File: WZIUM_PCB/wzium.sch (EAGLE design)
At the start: 5 parts, among them J2 RASPBERRYPI-40-PIN-GPIO_PTH_M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

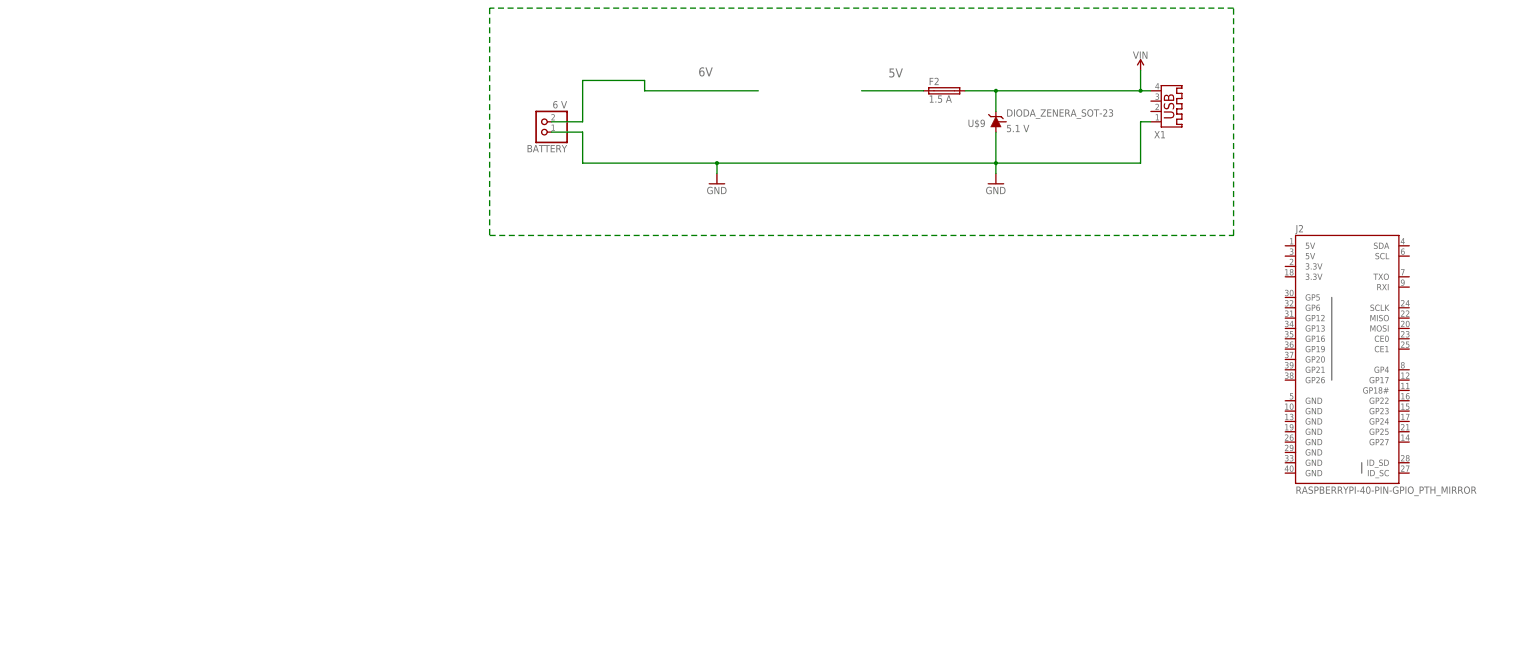
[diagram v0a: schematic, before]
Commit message: dodanie sekcji sterowania silnikiem i AVR, dodanie .gitignore
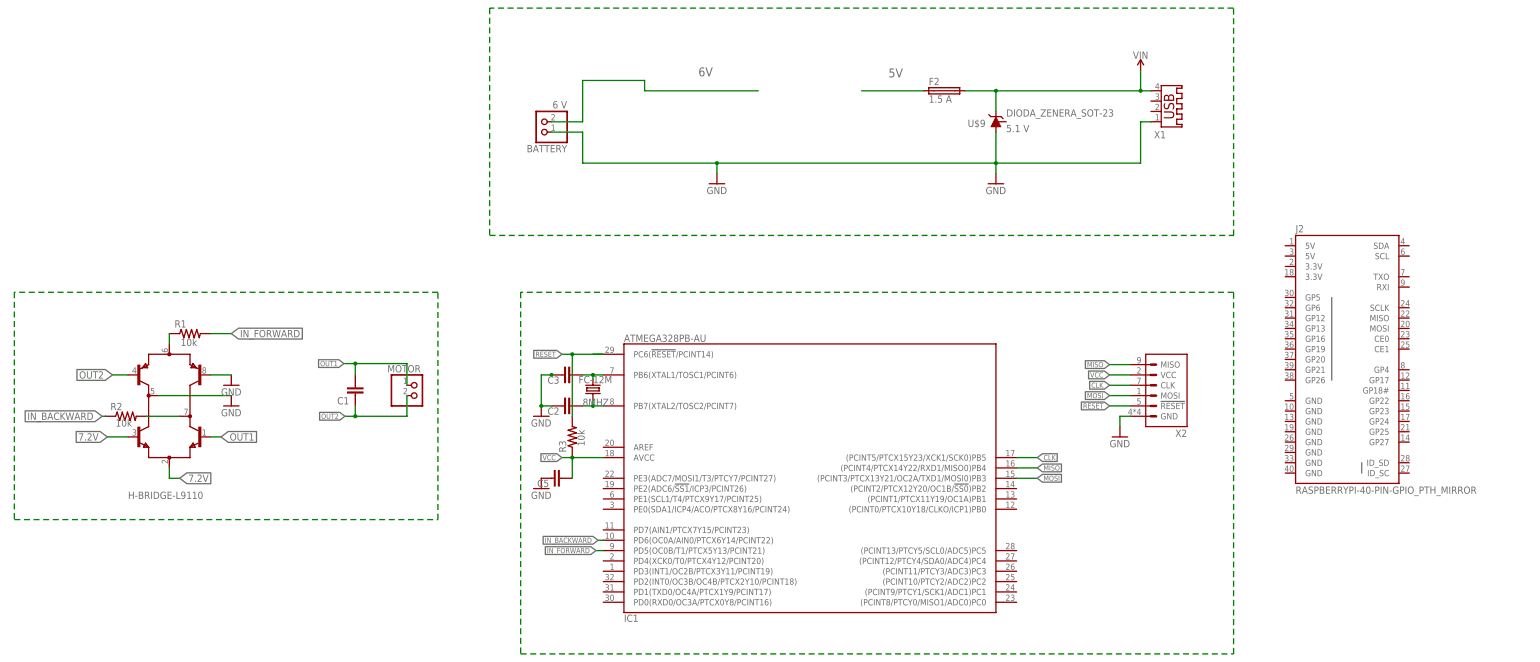
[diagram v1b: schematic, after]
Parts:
- added 8MHZ: FC-12M, crystal:FC-12M
- added C1, C2, C3, C5: (no value), rcl:C-EUC0805
- added H-BRIDGE-L9110: (no value), zetex:H-BRIDGE
- added IC1: ATMEGA328PB-AU, atmel:ATMEGA328PB-AU
- added MOTOR: (no value), DC_LOAD_AU:PINHD-1X2
- added R1, R2, R3: 10k, rcl:R-US_R0805
- added X2: (no value), atmel:MISO_MOSIIDC-10V
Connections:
- new net 7.2V: H-BRIDGE-L9110.B2, H-BRIDGE-L9110.E2E3
- new net CLK: IC1G$1.(PCINT5/PTCX15Y23/XCK1/SCK0)PB5, X2.CLK
- new net IN_BACKWARD: IC1G$1.PD6(OC0A/AIN0/PTCX6Y14/PCINT22), R2.1
- new net IN_FORWARD: IC1G$1.PD5(OC0B/T1/PTCX5Y13/PCINT21), R1.2
- new net MISO: IC1G$1.(PCINT4/PTCX14Y22/RXD1/MISO0)PB4, X2.MISO
- new net MOSI: IC1G$1.(PCINT3/PTCX13Y21/OC2A/TXD1/MOSI0)PB3, X2.MOSI
- new net N$3: H-BRIDGE-L9110.C3C4, R2.2
- new net N$5: H-BRIDGE-L9110.E1E4, R1.1
- new net N$7: 8MHZ.1, C3.1, IC1G$1.PB6(XTAL1/TOSC1/PCINT6)
- new net N$8: 8MHZ.2, C2.1, IC1G$1.PB7(XTAL2/TOSC2/PCINT7)
- new net OUT1: C1.2, H-BRIDGE-L9110.B3, MOTOR.1
- new net OUT2: C1.1, H-BRIDGE-L9110.B1, MOTOR.2
- new net RESET: IC1G$1.PC6(!RESET!/PCINT14), R3.2, X2.!RESET
- new net VCC: C5.1, IC1G$1.AVCC, R3.1, X2.VCC
- net GND: now also C2.2, C3.2, C5.2, H-BRIDGE-L9110.B4, H-BRIDGE-L9110.C1C2, X2.GND
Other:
- note added: "AVR Controller Section"
- note added: "DC Driver Section"
- note added: "RPi Power Section"
- note removed: "ZASILANIE RPi"

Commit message: dodano sekcje czujnikow odleglosci Sharp GP2Y0A41SK0F
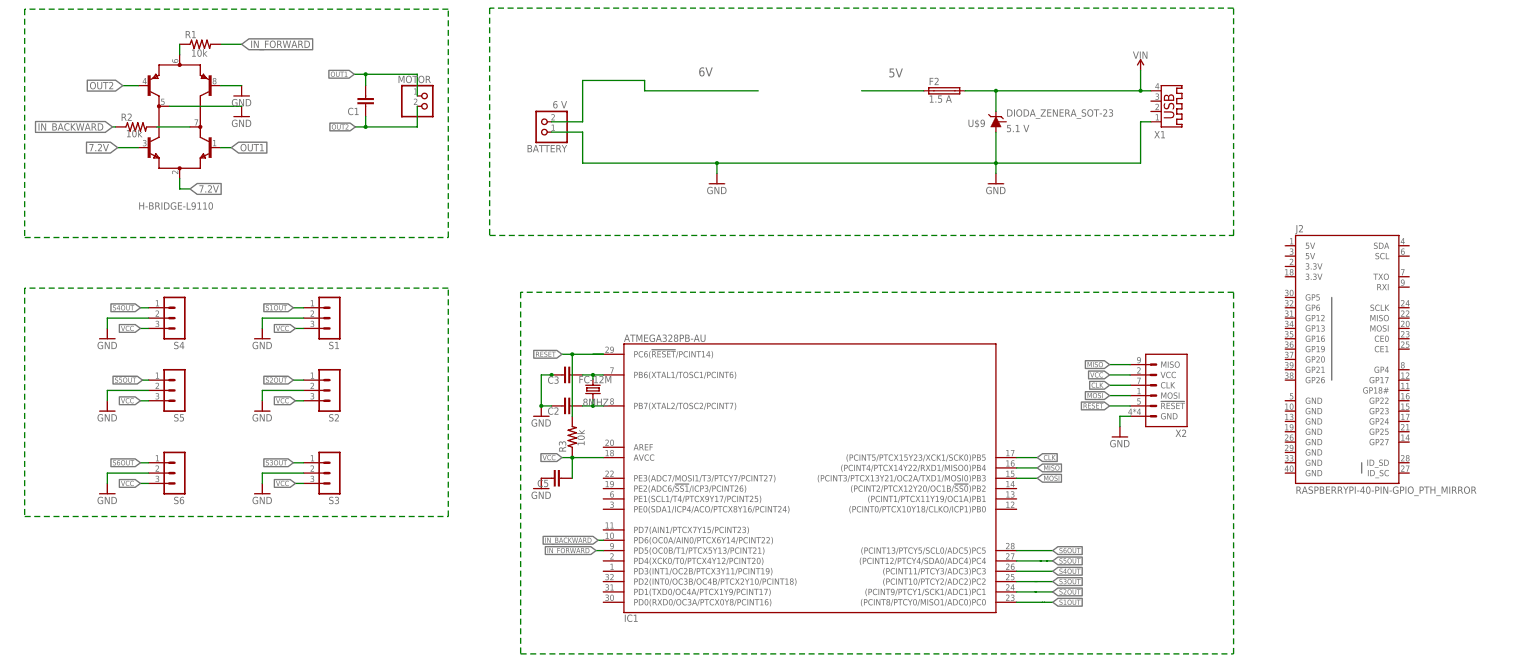
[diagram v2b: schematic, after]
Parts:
- added S1, S2, S3, S4, S5, S6: (no value), con-lstb:MA03-1
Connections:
- new net S1OUT: IC1G$1.(PCINT8/PTCY0/MISO1/ADC0)PC0, S1.1
- new net S2OUT: IC1G$1.(PCINT9/PTCY1/SCK1/ADC1)PC1, S2.1
- new net S3OUT: IC1G$1.(PCINT10/PTCY2/ADC2)PC2, S3.1
- new net S4OUT: IC1G$1.(PCINT11/PTCY3/ADC3)PC3, S4.1
- new net S5OUT: IC1G$1.(PCINT12/PTCY4/SDA0/ADC4)PC4, S5.1
- new net S6OUT: IC1G$1.(PCINT13/PTCY5/SCL0/ADC5)PC5, S6.1
- net GND: now also S1.2, S2.2, S3.2, S4.2, S5.2, S6.2
- net VCC: now also S1.3, S2.3, S3.3, S4.3, S5.3, S6.3
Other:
- note added: "Distance Sensors Section"
- moved on the sheet: C1, H-BRIDGE-L9110, MOTOR, R1, R2
